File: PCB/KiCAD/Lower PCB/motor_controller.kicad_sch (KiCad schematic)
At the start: 43 parts, among them M1 Conn_01x02_Pin, M2 Conn_01x02_Pin, M3 Conn_01x02_Pin, M4 Conn_01x02_Pin, U2 LMD18200, U3 LMD18200, U4 LMD18200, U5 LMD18200, U6 ATmega328PB-A, Y2 Crystal

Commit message: Placed components on Lower PCB
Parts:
- added R8: 10k, Resistor_SMD:R_0805_2012Metric_Pad1.20x1.40mm_HandSolder, symbol Device:R
- M1, M2, M3, M4: footprint Connector_Molex:Molex_KK-254_AE-6410-02A_1x02_P2.54mm_Vertical -> Connector_JST:JST_XH_B2B-XH-A_1x02_P2.50mm_Vertical
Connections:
- net +5V: now also R8.1
- net at U6.29 (~{RESET}/PC6): now also R8.2
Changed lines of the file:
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@@
 	(wire
 		(pts
+			(xy 86.36 83.82) (xy 86.36 85.09)
+		)
+		(stroke
+			(width 0)
+			(type default)
+		)
+	)
+	(wire
+		(pts
 			(xy 158.75 93.98) (xy 158.75 92.71)
 		)
@@
 	(wire
 		(pts
+			(xy 62.23 83.82) (xy 86.36 83.82)
+		)
+		(stroke
+			(width 0)
+			(type default)
+		)
+	)
+	(wire
+		(pts
 			(xy 30.48 45.72) (xy 31.75 45.72)
 		)
@@
 	(wire
 		(pts
+			(xy 86.36 92.71) (xy 86.36 95.25)
+		)
+		(stroke
+			(width 0)
+			(type default)
+		)
+	)
+	(wire
+		(pts
 			(xy 96.52 41.91) (xy 96.52 39.37)
 		)
@@
 			)
 		)
-		(property "Footprint" "Connector_Molex:Molex_KK-254_AE-6410-02A_1x02_P2.54mm_Vertical"
+		(property "Footprint" "Connector_JST:JST_XH_B2B-XH-A_1x02_P2.50mm_Vertical"
 			(at 189.23 123.19 0)
 			(effects
@@
 	)
 	(symbol
+		(lib_id "Device:R")
+		(at 86.36 88.9 180)
+		(unit 1)
+		(exclude_from_sim no)
+		(in_bom yes)
+		(on_board yes)
+		(dnp no)
+		(property "Reference" "R8"
+			(at 88.9 87.6299 0)
+			(effects
+				(font
+					(size 1.27 1.27)
+				)
+				(justify right)
+			)
+		)
+		(property "Value" "10k"
+			(at 88.9 90.1699 0)
+			(effects
+				(font
+					(size 1.27 1.27)
+				)
+				(justify right)
+			)
+		)
+		(property "Footprint" "Resistor_SMD:R_0805_2012Metric_Pad1.20x1.40mm_HandSolder"
+			(at 88.138 88.9 90)
+			(effects
+				(font
+					(size 1.27 1.27)
+				)
+				(hide yes)
+			)
+		)
+		(property "Datasheet" "~"
+			(at 86.36 88.9 0)
+			(effects
+				(font
+					(size 1.27 1.27)
+				)
+				(hide yes)
+			)
+		)
+		(property "Description" "Resistor"
+			(at 86.36 88.9 0)
+			(effects
+				(font
+					(size 1.27 1.27)
+				)
+				(hide yes)
+			)
+		)
+		(pin "1"
+		)
+		(pin "2"
+		)
+		(instances
+			(project "Lower PCB"
+				(path "/ce5ddd0c-e3c7-41d2-82e8-7cf5c6a3a2a3/5ff91d1b-d345-4f28-b2f0-8a2ac55be9dc"
+					(reference "R8")
+					(unit 1)
+				)
+			)
+		)
+	)
+	(symbol
 		(lib_id "Connector:Conn_01x02_Pin")
 		(at 189.23 53.34 180)
@@
 			)
 		)
-		(property "Footprint" "Connector_Molex:Molex_KK-254_AE-6410-02A_1x02_P2.54mm_Vertical"
+		(property "Footprint" "Connector_JST:JST_XH_B2B-XH-A_1x02_P2.50mm_Vertical"
 			(at 189.23 53.34 0)
 			(effects
@@
 			)
 		)
-		(property "Footprint" "Connector_Molex:Molex_KK-254_AE-6410-02A_1x02_P2.54mm_Vertical"
+		(property "Footprint" "Connector_JST:JST_XH_B2B-XH-A_1x02_P2.50mm_Vertical"
 			(at 274.32 53.34 0)
 			(effects
@@
 	)
 	(symbol
+		(lib_id "power:+5V")
+		(at 86.36 95.25 180)
+		(unit 1)
+		(exclude_from_sim no)
+		(in_bom yes)
+		(on_board yes)
+		(dnp no)
+		(fields_autoplaced yes)
+		(property "Reference" "#PWR049"
+			(at 86.36 91.44 0)
+			(effects
+				(font
+					(size 1.27 1.27)
+				)
+				(hide yes)
+			)
+		)
+		(property "Value" "+5V"
+			(at 86.36 100.33 0)
+			(effects
+				(font
+					(size 1.27 1.27)
+				)
+			)
+		)
+		(property "Footprint" ""
+			(at 86.36 95.25 0)
+			(effects
+				(font
+					(size 1.27 1.27)
+				)
+				(hide yes)
+			)
+		)
+		(property "Datasheet" ""
+			(at 86.36 95.25 0)
+			(effects
+				(font
+					(size 1.27 1.27)
+				)
+				(hide yes)
+			)
+		)
+		(property "Description" "Power symbol creates a global label with name \"+5V\""
+			(at 86.36 95.25 0)
+			(effects
+				(font
+					(size 1.27 1.27)
+				)
+				(hide yes)
+			)
+		)
+		(pin "1"
+		)
+		(instances
+			(project "Lower PCB"
+				(path "/ce5ddd0c-e3c7-41d2-82e8-7cf5c6a3a2a3/5ff91d1b-d345-4f28-b2f0-8a2ac55be9dc"
+					(reference "#PWR049")
+					(unit 1)
+				)
+			)
+		)
+	)
+	(symbol
 		(lib_id "Device:C")
 		(at 175.26 128.27 0)
@@
 			)
 		)
-		(property "Footprint" "Connector_Molex:Molex_KK-254_AE-6410-02A_1x02_P2.54mm_Vertical"
+		(property "Footprint" "Connector_JST:JST_XH_B2B-XH-A_1x02_P2.50mm_Vertical"
 			(at 274.32 123.19 0)
 			(effects

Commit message: More work to the lower PCB
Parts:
- removed Y2: Crystal, Crystal:Crystal_SMD_3225-4Pin_3.2x2.5mm_HandSoldering, symbol Device:Crystal
- added Y2: Crystal_GND24, Crystal:Crystal_SMD_5032-4Pin_5.0x3.2mm, symbol Device:Crystal_GND24
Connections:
- net at C23.2, U6.7 (XTAL1/PB6): now also Y2.1
- net at C24.2, U6.8 (XTAL2/PB7): now also Y2.3
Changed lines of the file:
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@@
 	(paper "A4")
 	(junction
+		(at 97.79 57.15)
+		(diameter 0)
+		(color 0 0 0 0)
+	)
+	(junction
 		(at 236.22 92.71)
 		(diameter 0)
@@
 	)
 	(junction
-		(at 87.63 58.42)
-		(diameter 0)
-		(color 0 0 0 0)
-	)
-	(junction
 		(at 27.94 34.29)
 		(diameter 0)
@@
 	)
 	(junction
+		(at 87.63 57.15)
+		(diameter 0)
+		(color 0 0 0 0)
+	)
+	(junction
 		(at 236.22 22.86)
 		(diameter 0)
@@
 	)
 	(junction
-		(at 97.79 58.42)
-		(diameter 0)
-		(color 0 0 0 0)
-	)
-	(junction
 		(at 175.26 111.76)
 		(diameter 0)
@@
 	(wire
 		(pts
-			(xy 96.52 58.42) (xy 97.79 58.42)
+			(xy 236.22 22.86) (xy 236.22 36.83)
 		)
 		(stroke
@@
 	(wire
 		(pts
-			(xy 236.22 22.86) (xy 236.22 36.83)
+			(xy 27.94 22.86) (xy 34.29 22.86)
 		)
 		(stroke
@@
 	(wire
 		(pts
-			(xy 27.94 22.86) (xy 34.29 22.86)
+			(xy 87.63 46.99) (xy 87.63 48.26)
 		)
 		(stroke
@@
 	(wire
 		(pts
-			(xy 87.63 46.99) (xy 87.63 48.26)
+			(xy 97.79 57.15) (xy 97.79 63.5)
 		)
 		(stroke
@@
 	(wire
 		(pts
-			(xy 97.79 63.5) (xy 97.79 58.42)
-		)
-		(stroke
-			(width 0)
-			(type default)
-		)
-	)
-	(wire
-		(pts
 			(xy 269.24 120.65) (xy 266.7 120.65)
 		)
@@
 	(wire
 		(pts
-			(xy 97.79 58.42) (xy 97.79 55.88)
+			(xy 97.79 55.88) (xy 97.79 57.15)
 		)
 		(stroke
@@
 	(wire
 		(pts
+			(xy 87.63 57.15) (xy 88.9 57.15)
+		)
+		(stroke
+			(width 0)
+			(type default)
+		)
+	)
+	(wire
+		(pts
 			(xy 260.35 67.31) (xy 260.35 69.85)
 		)
@@
 	(wire
 		(pts
-			(xy 62.23 81.28) (xy 64.77 81.28)
+			(xy 96.52 57.15) (xy 97.79 57.15)
 		)
 		(stroke
@@
 	(wire
 		(pts
-			(xy 40.64 33.02) (xy 40.64 34.29)
+			(xy 62.23 81.28) (xy 64.77 81.28)
 		)
 		(stroke
@@
 	(wire
 		(pts
-			(xy 96.52 21.59) (xy 96.52 22.86)
+			(xy 40.64 33.02) (xy 40.64 34.29)
 		)
 		(stroke
@@
 	(wire
 		(pts
-			(xy 87.63 58.42) (xy 88.9 58.42)
+			(xy 96.52 21.59) (xy 96.52 22.86)
 		)
 		(stroke
@@
 	(wire
 		(pts
+			(xy 87.63 57.15) (xy 87.63 60.96)
+		)
+		(stroke
+			(width 0)
+			(type default)
+		)
+	)
+	(wire
+		(pts
 			(xy 271.78 67.31) (xy 260.35 67.31)
 		)
@@
 	(wire
 		(pts
-			(xy 87.63 58.42) (xy 87.63 55.88)
+			(xy 87.63 55.88) (xy 87.63 57.15)
 		)
 		(stroke
@@
 	(wire
 		(pts
-			(xy 87.63 60.96) (xy 87.63 58.42)
-		)
-		(stroke
-			(width 0)
-			(type default)
-		)
-	)
-	(wire
-		(pts
 			(xy 269.24 50.8) (xy 266.7 50.8)
 		)
@@
 	)
 	(symbol
+		(lib_id "Device:Crystal_GND24")
+		(at 92.71 57.15 0)
+		(unit 1)
+		(exclude_from_sim no)
+		(in_bom yes)
+		(on_board yes)
+		(dnp no)
+		(property "Reference" "Y2"
+			(at 95.758 61.976 0)
+			(effects
+				(font
+					(size 1.27 1.27)
+				)
+			)
+		)
+		(property "Value" "Crystal_GND24"
+			(at 104.14 53.2698 0)
+			(effects
+				(font
+					(size 1.27 1.27)
+				)
+				(hide yes)
+			)
+		)
+		(property "Footprint" "Crystal:Crystal_SMD_5032-4Pin_5.0x3.2mm"
+			(at 92.71 57.15 0)
+			(effects
+				(font
+					(size 1.27 1.27)
+				)
+				(hide yes)
+			)
+		)
+		(property "Datasheet" "~"
+			(at 92.71 57.15 0)
+			(effects
+				(font
+					(size 1.27 1.27)
+				)
+				(hide yes)
+			)
+		)
+		(property "Description" "Four pin crystal, GND on pins 2 and 4"
+			(at 92.71 57.15 0)
+			(effects
+				(font
+					(size 1.27 1.27)
+				)
+				(hide yes)
+			)
+		)
+		(pin "1"
+		)
+		(pin "4"
+		)
+		(pin "2"
+		)
+		(pin "3"
+		)
+		(instances
+			(project ""
+				(path "/ce5ddd0c-e3c7-41d2-82e8-7cf5c6a3a2a3/5ff91d1b-d345-4f28-b2f0-8a2ac55be9dc"
+					(reference "Y2")
+					(unit 1)
+				)
+			)
+		)
+	)
+	(symbol
 		(lib_id "power:+5V")
 		(at 86.36 95.25 180)
@@
 					(unit 1)
 				)
-			)
-		)
-	)
-	(symbol
-		(lib_id "Device:Crystal")
-		(at 92.71 58.42 0)
-		(unit 1)
-		(exclude_from_sim no)
-		(in_bom yes)
-		(on_board yes)
-		(dnp no)
-		(property "Reference" "Y2"
-			(at 92.71 62.23 0)
-			(effects
-				(font
-					(size 1.27 1.27)
-				)
-			)
-		)
-		(property "Value" "Crystal"
-			(at 92.71 54.356 0)
-			(effects
-				(font
-					(size 1.27 1.27)
-				)
-			)
-		)
-		(property "Footprint" "Crystal:Crystal_SMD_3225-4Pin_3.2x2.5mm_HandSoldering"
-			(at 92.71 58.42 0)
-			(effects
-				(font
-					(size 1.27 1.27)
-				)
-				(hide yes)
-			)
-		)
-		(property "Datasheet" "~"
-			(at 92.71 58.42 0)
-			(effects
-				(font
-					(size 1.27 1.27)
-				)
-				(hide yes)
-			)
-		)
-		(property "Description" "Two pin crystal"
-			(at 92.71 58.42 0)
-			(effects
-				(font
-					(size 1.27 1.27)
-				)
-				(hide yes)
-			)
-		)
-		(pin "2"
-		)
-		(pin "1"
-		)
-		(instances
-			(project "Lower PCB"
-				(path "/ce5ddd0c-e3c7-41d2-82e8-7cf5c6a3a2a3/5ff91d1b-d345-4f28-b2f0-8a2ac55be9dc"
-					(reference "Y2")
-					(unit 1)
-				)

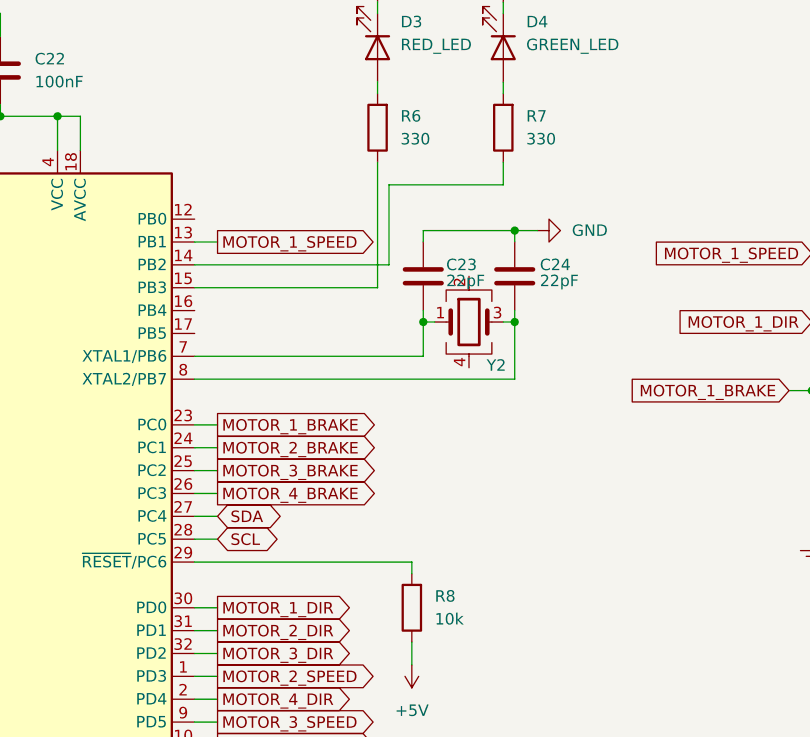
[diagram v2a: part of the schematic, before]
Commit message: Finished routing main motor controller connections and added connectors
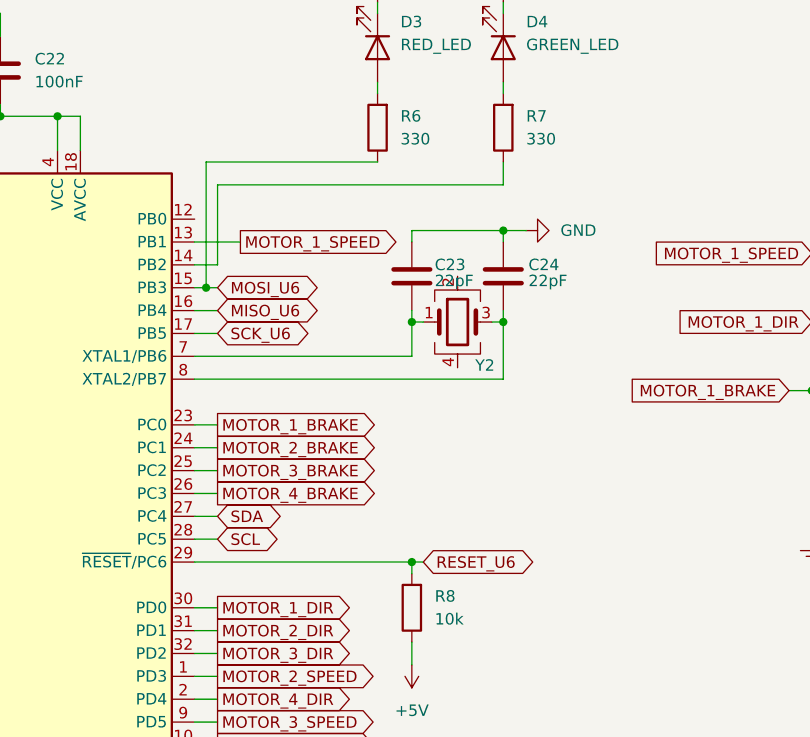
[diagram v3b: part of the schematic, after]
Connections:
- net Earth is gone; now on net GND: C12.2, C15.2, C16.2, C17.2, C18.2, C19.2, C27.2, C30.2, C6.2, C7.2, C8.2, C9.2, R1.2, R12.2, R13.2, R5.2, U2.4 (BRAKE), U2.7 (GND), U3.4 (BRAKE), U3.7 (GND), U4.4 (BRAKE), U4.7 (GND), U5.4 (BRAKE), U5.7 (GND), U6.23 (PC0), U6.24 (PC1), U6.25 (PC2), U6.26 (PC3)
- net MOSI_U6: now reaches R6.1, U6.15 (PB3)
- net RESET_U6: now reaches R8.2, U6.29 (~{RESET}/PC6)
- net MISO_U6: now reaches U6.16 (PB4)
- net SCK_U6: now reaches U6.17 (PB5)
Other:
- moved on the sheet: C23, C24, Y2

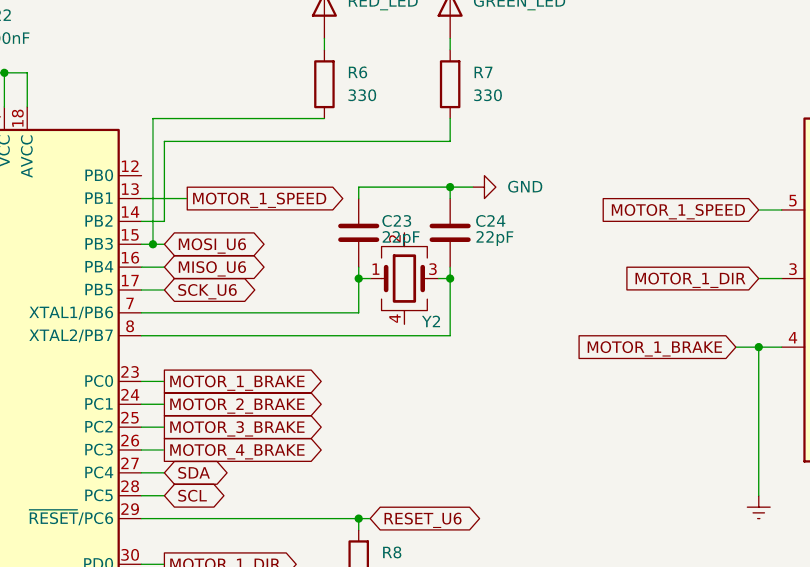
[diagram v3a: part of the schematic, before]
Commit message: More work to the Main PCB and refinement of Via sizes
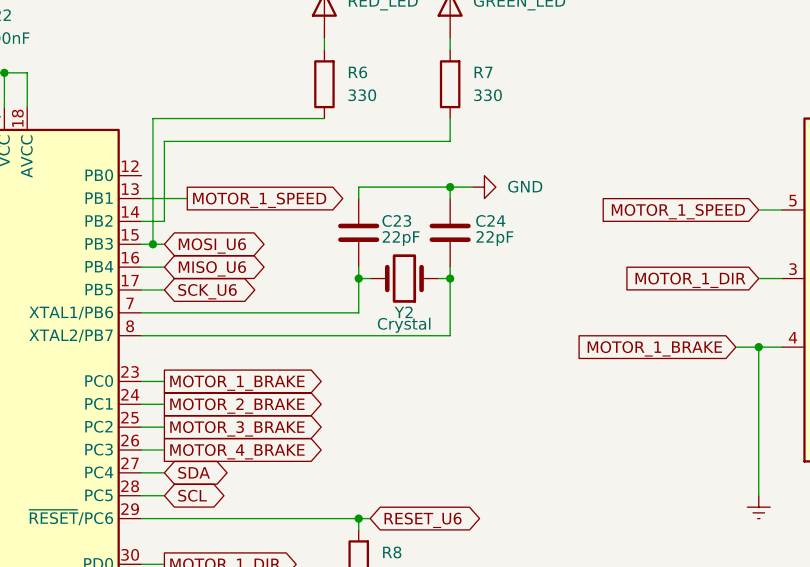
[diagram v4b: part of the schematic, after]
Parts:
- removed Y2: Crystal_GND24, Crystal:Crystal_SMD_5032-4Pin_5.0x3.2mm, symbol Device:Crystal_GND24
- added Y2: Crystal, Crystal:Crystal_SMD_HC49-SD, symbol Device:Crystal
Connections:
- net at C23.2, U6.7 (XTAL1/PB6): now also Y2.2
- net at C24.2, U6.8 (XTAL2/PB7): now also Y2.1
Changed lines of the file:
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@@
-	)
-	(symbol
-		(lib_id "Device:Crystal_GND24")
-		(at 91.44 57.15 0)
-		(unit 1)
-		(exclude_from_sim no)
-		(in_bom yes)
-		(on_board yes)
-		(dnp no)
-		(property "Reference" "Y2"
-			(at 94.488 61.976 0)
-			(effects
-				(font
-					(size 1.27 1.27)
-				)
-			)
-		)
-		(property "Value" "Crystal_GND24"
-			(at 102.87 53.2698 0)
-			(effects
-				(font
-					(size 1.27 1.27)
-				)
-				(hide yes)
-			)
-		)
-		(property "Footprint" "Crystal:Crystal_SMD_5032-4Pin_5.0x3.2mm"
-			(at 91.44 57.15 0)
-			(effects
-				(font
-					(size 1.27 1.27)
-				)
-				(hide yes)
-			)
-		)
-		(property "Datasheet" "~"
-			(at 91.44 57.15 0)
-			(effects
-				(font
-					(size 1.27 1.27)
-				)
-				(hide yes)
-			)
-		)
-		(property "Description" "Four pin crystal, GND on pins 2 and 4"
-			(at 91.44 57.15 0)
-			(effects
-				(font
-					(size 1.27 1.27)
-				)
-				(hide yes)
-			)
-		)
-		(pin "1"
-		)
-		(pin "4"
-		)
-		(pin "2"
-		)
-		(pin "3"
-		)
-		(instances
-			(project ""
-				(path "/ce5ddd0c-e3c7-41d2-82e8-7cf5c6a3a2a3/5ff91d1b-d345-4f28-b2f0-8a2ac55be9dc"
-					(reference "Y2")
-					(unit 1)
-				)
-			)
-		)
 	)
 	(symbol
@@
 					(unit 1)
 				)
+			)
+		)
+	)
+	(symbol
+		(lib_id "Device:Crystal")
+		(at 91.44 57.15 180)
+		(unit 1)
+		(exclude_from_sim no)
+		(in_bom yes)
+		(on_board yes)
+		(dnp no)
+		(property "Reference" "Y2"
+			(at 91.44 60.96 0)
+			(effects
+				(font
+					(size 1.27 1.27)
+				)
+			)
+		)
+		(property "Value" "Crystal"
+			(at 91.44 62.23 0)
+			(effects
+				(font
+					(size 1.27 1.27)
+				)
+			)
+		)
+		(property "Footprint" "Crystal:Crystal_SMD_HC49-SD"
+			(at 91.44 57.15 0)
+			(effects
+				(font
+					(size 1.27 1.27)
+				)
+				(hide yes)
+			)
+		)
+		(property "Datasheet" "~"
+			(at 91.44 57.15 0)
+			(effects
+				(font
+					(size 1.27 1.27)
+				)
+				(hide yes)
+			)
+		)
+		(property "Description" "Two pin crystal"
+			(at 91.44 57.15 0)
+			(effects
+				(font
+					(size 1.27 1.27)
+				)
+				(hide yes)
+			)
+		)
+		(pin "2"
+		)
+		(pin "1"
+		)
+		(instances
+			(project "Lower PCB"
+				(path "/ce5ddd0c-e3c7-41d2-82e8-7cf5c6a3a2a3/5ff91d1b-d345-4f28-b2f0-8a2ac55be9dc"
+					(reference "Y2")
+					(unit 1)
+				)

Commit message: Redone main PCB traces and started lower PCB
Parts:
- removed C10, C11, C13, C14, C20, C26, C28, C29: 10nF, Capacitor_SMD:C_1210_3225Metric_Pad1.33x2.70mm_HandSolder, symbol Device:C
- removed C12, C15, C18, C19, C27, C30, C8, C9: 0.1uF, Capacitor_SMD:C_0805_2012Metric_Pad1.18x1.45mm_HandSolder, symbol Device:C
- removed C16, C17, C6, C7: 220uF, Capacitor_SMD:CP_Elec_10x10, symbol Device:C_Polarized
- removed C21, C22, C25: 100nF, Capacitor_SMD:C_0805_2012Metric_Pad1.18x1.45mm_HandSolder, symbol Device:C
- removed C23, C24: 22pF, Capacitor_SMD:C_0805_2012Metric_Pad1.18x1.45mm_HandSolder, symbol Device:C
- removed D3: RED_LED, LED_SMD:LED_0805_2012Metric_Pad1.15x1.40mm_HandSolder, symbol Device:LED
- removed D4: GREEN_LED, LED_SMD:LED_0805_2012Metric_Pad1.15x1.40mm_HandSolder, symbol Device:LED
- removed M1, M2, M3, M4: Conn_01x02_Pin, Connector_JST:JST_XH_B2B-XH-A_1x02_P2.50mm_Vertical, symbol Connector:Conn_01x02_Pin
- removed R1, R12, R13, R5: 2.7k, Resistor_SMD:R_0805_2012Metric_Pad1.20x1.40mm_HandSolder, symbol Device:R
- removed R6, R7: 330, Resistor_SMD:R_0805_2012Metric_Pad1.20x1.40mm_HandSolder, symbol Device:R
- removed R8: 10k, Resistor_SMD:R_0805_2012Metric_Pad1.20x1.40mm_HandSolder, symbol Device:R
- removed U2, U3, U4, U5: LMD18200, Package_TO_SOT_THT:TO-220-11_P3.4x5.08mm_StaggerOdd_Lead4.58mm_Vertical, symbol Driver_Motor:LMD18200
- removed U6: ATmega328PB-A, Package_QFP:TQFP-32_7x7mm_P0.8mm, symbol MCU_Microchip_ATmega:ATmega328PB-A
- removed Y2: Crystal, Crystal:Crystal_SMD_HC49-SD, symbol Device:Crystal
